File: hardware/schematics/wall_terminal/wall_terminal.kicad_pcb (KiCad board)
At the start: 2 copper layers, 34.5 x 39.4 mm, 27 parts, among them J1 6P6C, J2 6P6C, J3 Conn_02x12_Odd_Even, J4 Reset, Q1 2N7000, U1 ATtiny13A-P, U2 MAX487E

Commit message: !refactor
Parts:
- removed JP1: INT/ADC, Jumper:SolderJumper-3_P1.3mm_Open_Pad1.0x1.5mm
- removed JP2: PWM/SIMPLE, Jumper:SolderJumper-3_P1.3mm_Open_Pad1.0x1.5mm
- removed Q1: 2N7000, Package_TO_SOT_THT:TO-92_Inline
- removed REF** (x4): SolderJumper-3_P1.3mm_Open_Pad1.0x1.5mm, Jumper:SolderJumper-3_P1.3mm_Open_Pad1.0x1.5mm
- R10: value R -> 1k
- R11: value R -> 120
- moved U2 10.8 mm to (146.6, 61.2), turned to 0 degrees
- moved U1 10.4 mm to (158.3, 61.2), turned to 0 degrees
- moved J4 3.89 mm to (175.5, 61.2)
- moved C1 2.51 mm to (174.8, 69.0), turned to 90 degrees
- moved G*** 0.25 mm to (162.1, 70.1)
- moved R10 0.25 mm to (149.4, 55.4)
- moved R9 0.17 mm to (152.5, 55.4)
- moved R8 0.10 mm to (155.7, 55.4)
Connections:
- net /SW_1 renamed /IN/S1
- net /SW_2 renamed /IN/S2
- net /SW_3 renamed /IN/S3
- net /SW_4 renamed /IN/S4
- net /SW_5 renamed /IN/S5
- net /SW_6 renamed /IN/S6
- net /SW_7 renamed /IN/S7
- net /SW_8 renamed /IN/S8
- net Net-(J4-Pin_2) renamed /MCU/~{RST}
- J3 pad 1: /LED+ -> /MCU/PWM_B
- J3 pad 2: /LED- -> GND
- J3 pad 3: +5V -> /MCU/PWM_A
- R1 pad 2: Net-(JP1-C) -> /IN/ADC
- R10 pad 1: +5V -> Net-(U2-RO)
- R10 pad 2: /LED+ -> /MCU/RX/TX
- R11 pad 1: /RS485_B -> /RS485_A
- R11 pad 2: /RS485_A -> /RS485_B
- R2 pad 2: Net-(JP1-C) -> /IN/ADC
- R3 pad 2: Net-(JP1-C) -> /IN/ADC
- R4 pad 2: Net-(JP1-C) -> /IN/ADC
- R5 pad 2: Net-(JP1-C) -> /IN/ADC
- R6 pad 2: Net-(JP1-C) -> /IN/ADC
- R7 pad 2: Net-(JP1-C) -> /IN/ADC
- R8 pad 2: Net-(JP1-C) -> /IN/ADC
- R9 pad 2: Net-(JP1-C) -> /IN/ADC
- U1 pad 2: /PB3 -> /MCU/DE/~{RE}
- U1 pad 3: /PB4 -> /MCU/RX/TX
- U1 pad 5: /PB0 -> /MCU/PWM_A
- U1 pad 6: /PB1 -> /MCU/PWM_B
- U1 pad 7: /PB2 -> /IN/ADC
- U2 pad 1: /PB3 -> Net-(U2-RO)
- U2 pad 2: /PB0 -> /MCU/DE/~{RE}
- U2 pad 3: /PB0 -> /MCU/DE/~{RE}
- U2 pad 4: /PB4 -> /MCU/RX/TX
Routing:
- net /LED-: track 45.4 -> 0.00 mm
- net /IN/ADC: track 0.00 -> 31.4 mm
- net /MCU/PWM_A: track 0.00 -> 29.6 mm, vias 0 -> 1
- net Net-(JP1-C): track 28.5 -> 0.00 mm
- net /MCU/PWM_B: track 0.00 -> 27.3 mm
- net /MCU/RX/TX: track 0.00 -> 22.3 mm, vias 0 -> 1
- net Net-(JP2-C): track 19.3 -> 0.00 mm
- net /MCU/DE/~{RE}: track 0.00 -> 15.9 mm
- net +5V: track 77.4 -> 62.3 mm
- net /PB4: track 12.1 -> 0.00 mm
- net /PB3: track 12.1 -> 0.00 mm
- net /PB2: track 9.73 -> 0.00 mm, vias 1 -> 0
- net /LED+: track 9.13 -> 0.00 mm
- net Net-(U2-RO): track 0.00 -> 8.17 mm
- net /PB0: track 7.03 -> 0.00 mm
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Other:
- board text removed: "IN Analog OUT PWM"
- board text removed: "IN Interrrupt OUT High/Low"

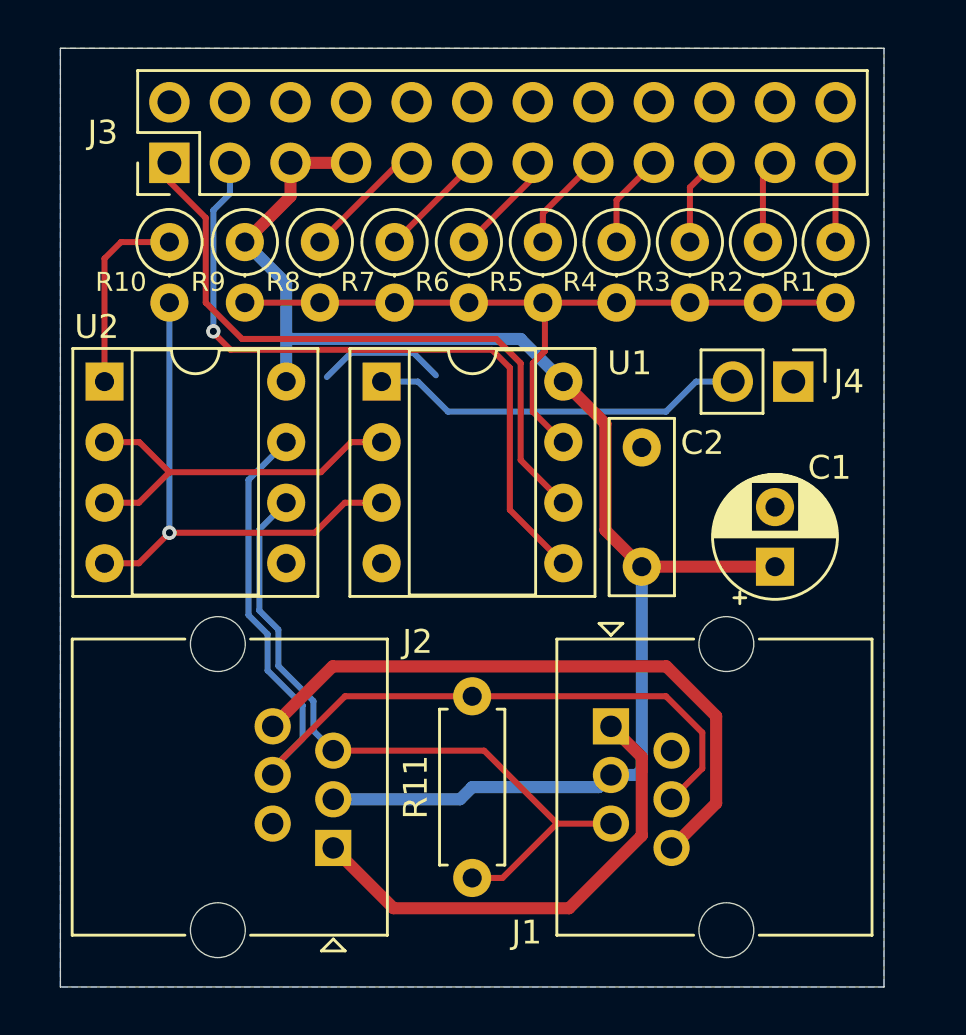
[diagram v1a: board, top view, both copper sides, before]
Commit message: fix: added optional resistors on PWM outputs.
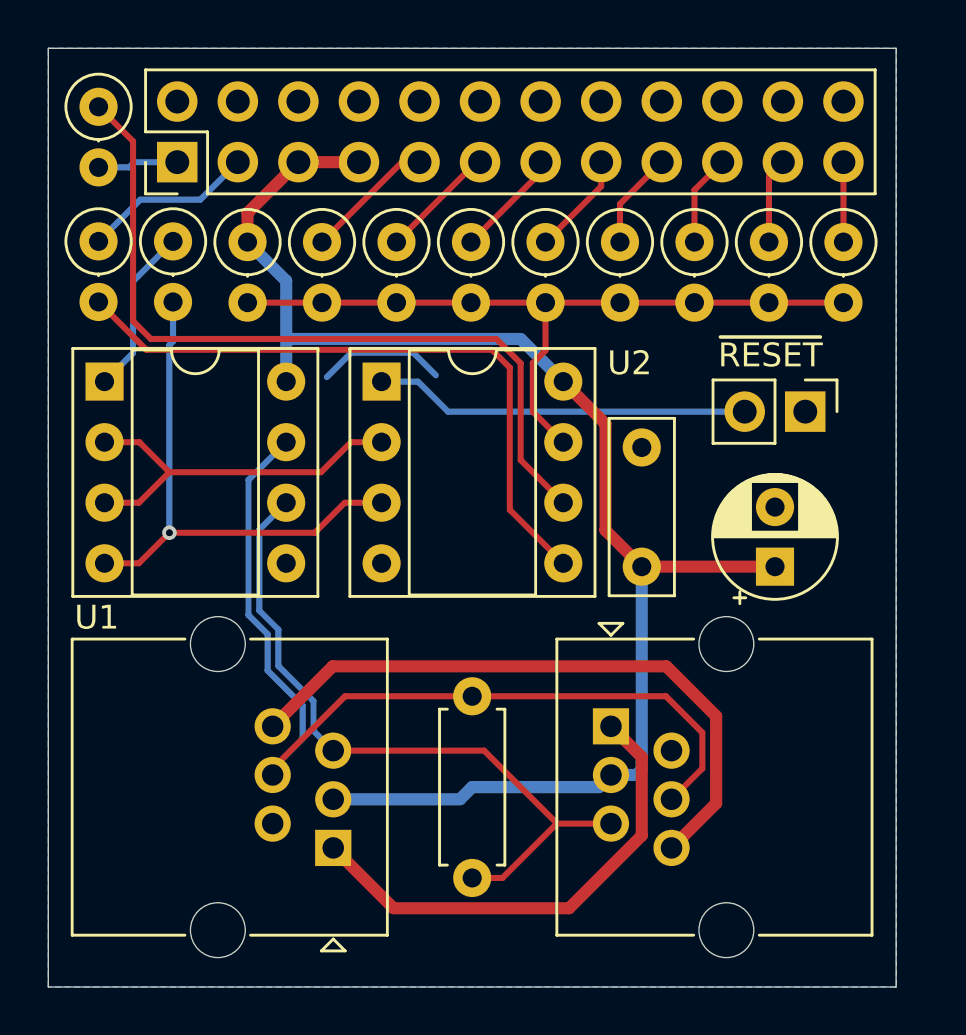
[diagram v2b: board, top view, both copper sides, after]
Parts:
- added R1: R, Resistor_THT:R_Axial_DIN0207_L6.3mm_D2.5mm_P2.54mm_Vertical, F.Cu at (146.4, 55.3)
- added R2: R, Resistor_THT:R_Axial_DIN0207_L6.3mm_D2.5mm_P2.54mm_Vertical, F.Cu at (146.4, 49.7)
- moved J1 1.36 mm to (176.0, 62.5)
- moved J2 0.33 mm to (149.7, 52.0)
- moved R3 0.33 mm to (177.6, 55.4)
- moved R4 0.25 mm to (174.5, 55.4)
- moved R5 0.19 mm to (171.4, 55.4)
- moved R12 0.16 mm to (149.5, 55.3)
- moved R6 0.14 mm to (168.2, 55.4)
- moved R11 0.11 mm to (152.6, 55.4)
- moved R7 0.11 mm to (165.1, 55.4)
- moved R10 0.09 mm to (155.8, 55.4)
- moved R8 0.09 mm to (162.0, 55.4)
- moved R9 0.08 mm to (158.9, 55.4)
- renumbered J4 to J1, J3 to J2, J2 to J3, J1 to J4, R8 to R10, R9 to R11, R10 to R12, R11 to R13, R1 to R3, R2 to R4, R3 to R5, R4 to R6, R5 to R7, R6 to R8, R7 to R9, U2 to U1, U1 to U2
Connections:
- J2 pad 1: /MCU/PWM_B -> Net-(J2-Pin_1)
- J2 pad 3: /MCU/PWM_A -> Net-(J2-Pin_3)
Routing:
- net Net-(J2-Pin_3): track 0.00 -> 7.22 mm
- net /MCU/PWM_B: track 27.3 -> 33.2 mm
- net Net-(J2-Pin_1): track 0.00 -> 3.39 mm
- net /MCU/PWM_A: track 29.6 -> 27.5 mm, vias 1 -> 0
- net Net-(U1-RO): track 8.17 -> 7.07 mm
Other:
- board size 34.5 x 39.4 mm -> 35.6 x 39.4 mm
- board text added: "~{RESET}"

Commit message: refactor
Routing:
- net GND: track 5.38 -> 0.00 mm
- net /RS485_B: track 39.6 -> 44.0 mm, vias 0 -> 2
- net Net-(U1-RO): track 7.07 -> 10.3 mm, vias 0 -> 2
- net /MCU/~{RST}: track 15.8 -> 17.5 mm, vias 0 -> 2
- net /MCU/RX/TX: track 22.4 -> 23.2 mm, vias 1 -> 3
- net /RS485_A: track 29.6 -> 30.3 mm, vias 0 -> 3
- net Net-(J2-Pin_3): track 7.22 -> 7.89 mm, vias 0 -> 1
- net /MCU/PWM_A: track 27.5 -> 28.0 mm, vias 0 -> 4
- net /MCU/PWM_B: track 33.2 -> 33.5 mm, vias 0 -> 4
